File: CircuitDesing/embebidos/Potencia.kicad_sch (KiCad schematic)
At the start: 5 parts

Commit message: Huellas parciales
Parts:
- C4: footprint (none) -> Capacitor_SMD:C_0603_1608Metric_Pad1.08x0.95mm_HandSolder
- gave numbers to parts that had none: 4
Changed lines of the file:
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@@
       (effects (font (size 1.27 1.27)) (justify left))
     )
-    (property "Footprint" "" (id 2) (at 116.5352 69.85 0)
+    (property "Footprint" "Capacitor_SMD:C_0603_1608Metric_Pad1.08x0.95mm_HandSolder" (id 2) (at 116.5352 69.85 0)
       (effects (font (size 1.27 1.27)) hide)
     )
@@
   (symbol (lib_id "Diode:1N5822") (at 86.36 74.93 270) (unit 1)
     (in_bom yes) (on_board yes) (fields_autoplaced)
-    (property "Reference" "D?" (id 0) (at 88.9 73.3424 90)
+    (property "Reference" "D4" (id 0) (at 88.9 73.3424 90)
       (effects (font (size 1.27 1.27)) (justify left))
     )
@@
   (symbol (lib_id "Diode:1N5822") (at 67.31 58.42 270) (unit 1)
     (in_bom yes) (on_board yes) (fields_autoplaced)
-    (property "Reference" "D?" (id 0) (at 69.85 56.8324 90)
+    (property "Reference" "D1" (id 0) (at 69.85 56.8324 90)
       (effects (font (size 1.27 1.27)) (justify left))
     )
@@
   (symbol (lib_id "power:GND") (at 78.74 85.09 0) (unit 1)
     (in_bom yes) (on_board yes) (fields_autoplaced)
-    (property "Reference" "#PWR?" (id 0) (at 78.74 91.44 0)
+    (property "Reference" "#PWR016" (id 0) (at 78.74 91.44 0)
       (effects (font (size 1.27 1.27)) hide)
     )
@@
   (symbol (lib_id "Diode:1N5822") (at 67.31 74.93 270) (unit 1)
     (in_bom yes) (on_board yes) (fields_autoplaced)
-    (property "Reference" "D?" (id 0) (at 69.85 73.3424 90)
+    (property "Reference" "D3" (id 0) (at 69.85 73.3424 90)
       (effects (font (size 1.27 1.27)) (justify left))
     )
@@
   (symbol (lib_id "Diode:1N5822") (at 86.36 58.42 270) (unit 1)
     (in_bom yes) (on_board yes) (fields_autoplaced)
-    (property "Reference" "D?" (id 0) (at 88.9 56.8324 90)
+    (property "Reference" "D2" (id 0) (at 88.9 56.8324 90)
       (effects (font (size 1.27 1.27)) (justify left))
     )

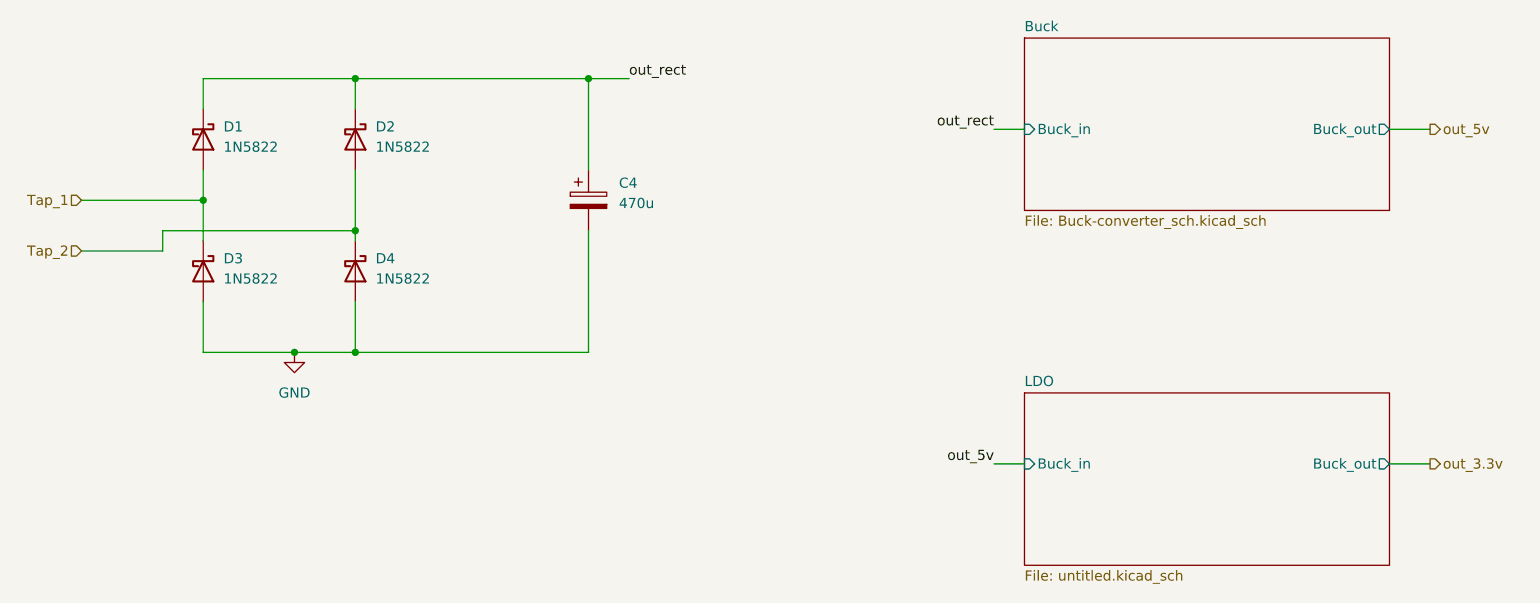
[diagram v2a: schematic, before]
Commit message: pull up
Circuito LDR
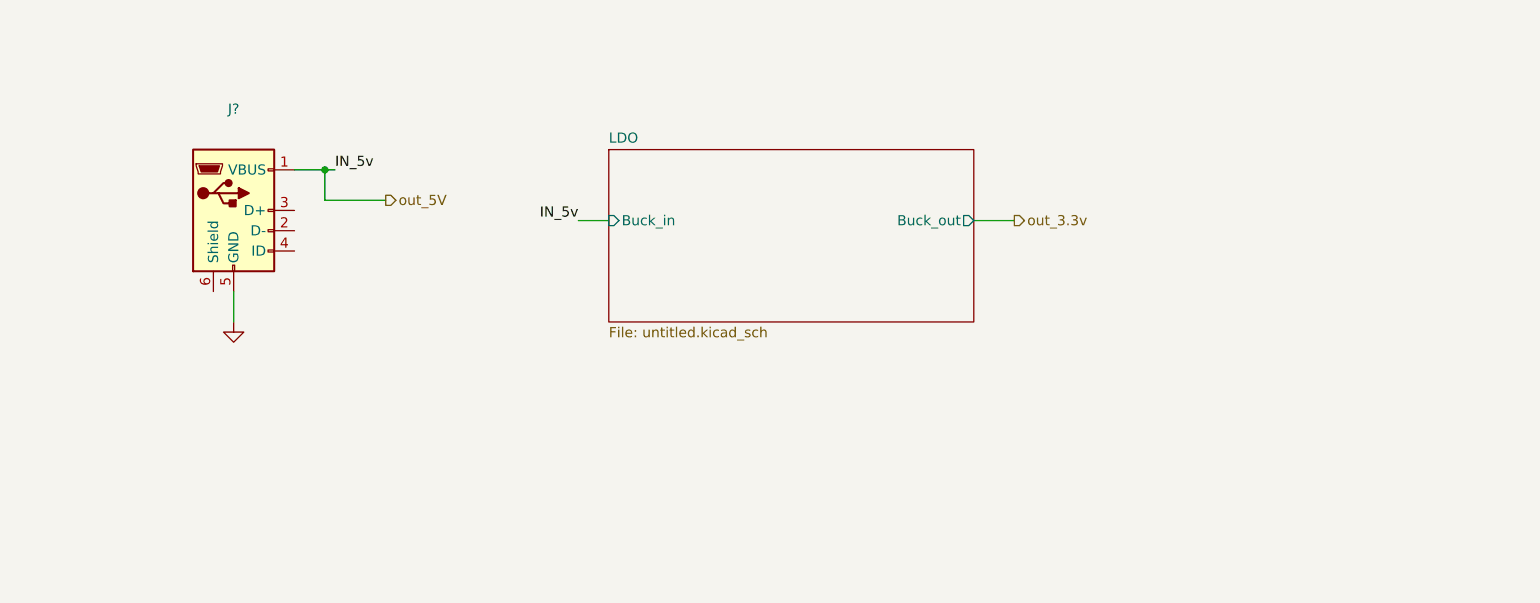
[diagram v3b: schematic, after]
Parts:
- removed C4: 470u, Capacitor_SMD:C_0603_1608Metric_Pad1.08x0.95mm_HandSolder, symbol Device:C_Polarized
- removed D1, D2, D3, D4: 1N5822, Diode_THT:D_DO-201AD_P15.24mm_Horizontal, symbol Diode:1N5822
- added J?: (no value), symbol Connector:USB_B_Micro
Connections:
- net GND: now also J?.5 (GND)
- new net out_5V: J?.1 (VBUS)
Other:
- removed sheet Buck

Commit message: Actualizacion huellas
Huellas+Programador
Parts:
- J2: renamed from J?; value (none) -> USB_B_Micro; footprint (none) -> Connector_USB:USB_Micro-B_Amphenol_10118194_Horizontal
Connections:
- no-connect marks 0 -> 4
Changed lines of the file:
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@@
   (junction (at 82.55 62.23) (diameter 0) (color 0 0 0 0)
   )
+  (no_connect (at 78.74 69.85))
+  (no_connect (at 78.74 72.39))
+  (no_connect (at 68.58 77.47))
+  (no_connect (at 78.74 67.31))
   (wire (pts (xy 82.55 62.23) (xy 82.55 66.04))
     (stroke (width 0) (type default) (color 0 0 0 0))
   )
-  (wire (pts (xy 82.55 62.23) (xy 83.82 62.23))
+  (wire (pts (xy 82.55 62.23) (xy 91.44 62.23))
     (stroke (width 0) (type default) (color 0 0 0 0))
   )
@@
     (stroke (width 0) (type default) (color 0 0 0 0))
   )
-  (wire (pts (xy 163.83 68.58) (xy 168.91 68.58))
+  (wire (pts (xy 139.7 64.77) (xy 144.78 64.77))
     (stroke (width 0) (type default) (color 0 0 0 0))
   )
@@
     (stroke (width 0) (type default) (color 0 0 0 0))
   )
-  (wire (pts (xy 114.3 68.58) (xy 118.11 68.58))
+  (wire (pts (xy 110.49 64.77) (xy 114.3 64.77))
     (stroke (width 0) (type default) (color 0 0 0 0))
   )
@@
     (stroke (width 0) (type default) (color 0 0 0 0))
   )
-  (label "IN_5v" (at 83.82 62.23 0)
+  (label "IN_5v" (at 91.44 62.23 0)
     (effects (font (size 1.27 1.27)) (justify left bottom))
   )
-  (label "IN_5v" (at 114.3 68.58 180)
+  (label "IN_5v" (at 110.49 64.77 180)
     (effects (font (size 1.27 1.27)) (justify right bottom))
   )
-  (hierarchical_label "out_3.3v" (shape output) (at 168.91 68.58 0)
+  (hierarchical_label "out_3.3v" (shape output) (at 144.78 64.77 0)
     (effects (font (size 1.27 1.27)) (justify left))
   )
@@
   (symbol (lib_id "power:GND") (at 71.12 81.28 0) (unit 1)
     (in_bom yes) (on_board yes) (fields_autoplaced)
-    (property "Reference" "#PWR?" (id 0) (at 71.12 87.63 0)
+    (property "Reference" "#PWR0108" (id 0) (at 71.12 87.63 0)
       (effects (font (size 1.27 1.27)) hide)
     )
-    (property "Value" "" (id 1) (at 71.12 86.36 0))
+    (property "Value" "GND" (id 1) (at 71.12 86.36 0))
     (property "Footprint" "" (id 2) (at 71.12 81.28 0)
       (effects (font (size 1.27 1.27)) hide)
@@
   (symbol (lib_id "Connector:USB_B_Micro") (at 71.12 67.31 0) (unit 1)
     (in_bom yes) (on_board yes) (fields_autoplaced)
-    (property "Reference" "J?" (id 0) (at 71.12 54.61 0))
-    (property "Value" "" (id 1) (at 71.12 57.15 0))
-    (property "Footprint" "" (id 2) (at 74.93 68.58 0)
+    (property "Reference" "J2" (id 0) (at 71.12 54.61 0))
+    (property "Value" "USB_B_Micro" (id 1) (at 71.12 57.15 0))
+    (property "Footprint" "Connector_USB:USB_Micro-B_Amphenol_10118194_Horizontal" (id 2) (at 74.93 68.58 0)
       (effects (font (size 1.27 1.27)) hide)
     )
@@
     (pin "6")
   )
-  (sheet (at 118.11 59.69) (size 45.72 21.59) (fields_autoplaced)
+  (sheet (at 114.3 62.23) (size 25.4 5.08) (fields_autoplaced)
     (stroke (width 0.1524) (type solid) (color 0 0 0 0))
     (fill (color 0 0 0 0.0000))
-    (property "Sheet name" "LDO" (id 0) (at 118.11 58.9784 0)
+    (property "Sheet name" "LDO" (id 0) (at 114.3 61.5184 0)
       (effects (font (size 1.27 1.27)) (justify left bottom))
     )
-    (property "Sheet file" "untitled.kicad_sch" (id 1) (at 118.11 81.8646 0)
+    (property "Sheet file" "untitled.kicad_sch" (id 1) (at 114.3 67.8946 0)
       (effects (font (size 1.27 1.27)) (justify left top))
     )
-    (pin "Buck_in" input (at 118.11 68.58 180)
+    (pin "Buck_in" input (at 114.3 64.77 180)
       (effects (font (size 1.27 1.27)) (justify left))
     )
-    (pin "Buck_out" output (at 163.83 68.58 0)
+    (pin "Buck_out" output (at 139.7 64.77 0)
       (effects (font (size 1.27 1.27)) (justify right))
     )

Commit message: Ruteo completo
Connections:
- net out_5V renamed 5V
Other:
- sheet LDO ports: added LDO_in, LDO_out; removed Buck_in, Buck_out
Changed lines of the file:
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@@
     (stroke (width 0) (type default) (color 0 0 0 0))
   )
-  (wire (pts (xy 82.55 62.23) (xy 91.44 62.23))
+  (wire (pts (xy 82.55 62.23) (xy 110.49 62.23))
+    (stroke (width 0) (type default) (color 0 0 0 0))
+  )
+  (wire (pts (xy 110.49 62.23) (xy 110.49 64.77))
     (stroke (width 0) (type default) (color 0 0 0 0))
   )
@@
     (stroke (width 0) (type default) (color 0 0 0 0))
   )
-  (label "IN_5v" (at 91.44 62.23 0)
-    (effects (font (size 1.27 1.27)) (justify left bottom))
-  )
-  (label "IN_5v" (at 110.49 64.77 180)
-    (effects (font (size 1.27 1.27)) (justify right bottom))
-  )
   (hierarchical_label "out_3.3v" (shape output) (at 144.78 64.77 0)
     (effects (font (size 1.27 1.27)) (justify left))
   )
-  (hierarchical_label "out_5V" (shape output) (at 90.17 66.04 0)
+  (hierarchical_label "5V" (shape output) (at 90.17 66.04 0)
     (effects (font (size 1.27 1.27)) (justify left))
   )
   (symbol (lib_id "power:GND") (at 71.12 81.28 0) (unit 1)
     (in_bom yes) (on_board yes) (fields_autoplaced)
-    (property "Reference" "#PWR0108" (id 0) (at 71.12 87.63 0)
+    (property "Reference" "#PWR028" (id 0) (at 71.12 87.63 0)
       (effects (font (size 1.27 1.27)) hide)
     )
@@
       (effects (font (size 1.27 1.27)) (justify left top))
     )
-    (pin "Buck_in" input (at 114.3 64.77 180)
+    (pin "LDO_out" output (at 139.7 64.77 0)
+      (effects (font (size 1.27 1.27)) (justify right))
+    )
+    (pin "LDO_in" input (at 114.3 64.77 180)
       (effects (font (size 1.27 1.27)) (justify left))
     )
-    (pin "Buck_out" output (at 139.7 64.77 0)
-      (effects (font (size 1.27 1.27)) (justify right))
-    )
   )
